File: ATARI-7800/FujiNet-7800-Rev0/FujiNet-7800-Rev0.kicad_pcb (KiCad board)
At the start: 6 copper layers, 72.4 x 115 mm, 135 parts, among them J1 Atari7800_Cart_Edge_32, J2 DBG UART, J3 microSD, J4 USB-C, Q1 2N7002, Q2 AO3401A, SW1 RESET, SW2 BOOTSEL, SW3 S3_RST, SW4 S3_BOOT, U1 RP2354B, U10 AP63203WU, U11 AP2112K-3.3, U2 74HCT14, U3 74HCT00, U4 74HCT20, U5 74HCT20, U6 AS6C4008-55TIN, U7 ESP32-S3-WROOM-1-N16R8, U8 CP2102N-A02-GQFN28, U9 UMH3N, Y1 12MHz

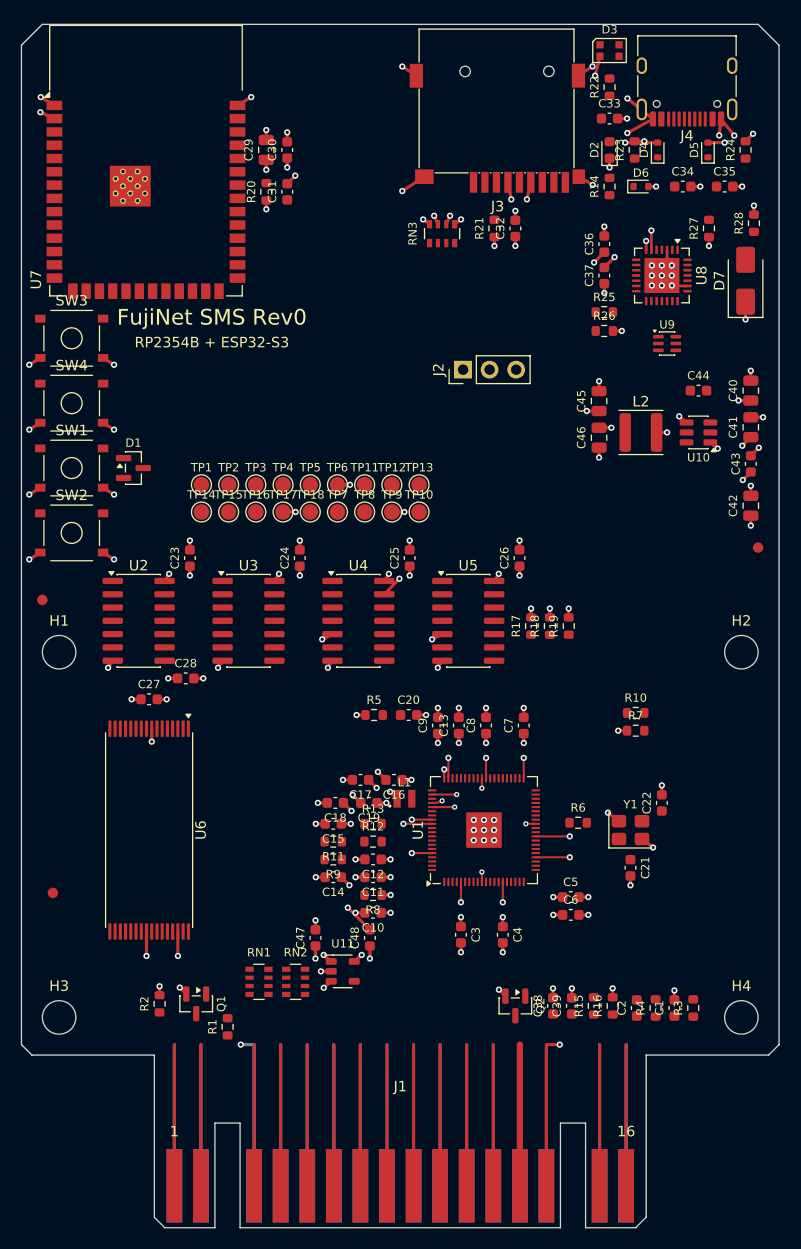
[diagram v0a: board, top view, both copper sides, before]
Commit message: ATARI-7800 Rev0: route the board, JLCPCB + PCBWay packages, layout review
- Routed 6-layer board: 117 nets; DRC 0/0/0 at every severity with schematic
  parity; check_vias clean. The D0-D7 100R packs now face the RP (rotation
  180, RN1 at x 85.5): with them the other way round, every route left
  RP_D5 open. route_board.sh defaults to the settings that routed it
  (12 Freerouting passes, hybrid strategy).
- Fab packages from one gerber set: exports/jlcpcb (BOM, CPL with measured
  rotations) and exports/pcbway (MPN BOM, centroid, assembly drawing).
- tools/audit/check_gerbers.py checks the fab zips against edge_geom.py:
  slots, both finger faces, mask windows, nothing in the tab. It runs in
  build_all.sh and run_pcb_audit.sh.
- Design review Part 2: routing, the variant runs, and the triage of every
  layout finding. README rewritten for the board, ordering and bring-up.
- R_HALT 10k on the board (sync_pcb_sheets now syncs value, MPN, LCSC and
  description). The audio level resistor is no longer marked provisional.
- Fixes:
  - check_vias tests round pads as circles;
  - gen_sch writes the right top-level sheet (it was the NES template's);
  - the silkscreen title read "FujiNet SMS Rev0";
  - the TS-1187A buttons get a 3D model (the TL3342's) in the library too;
  - PCBWay BOM lines describe the part, not one instance's function;
  - the unused placement variant B is dropped; the tab depth moves into
    edge_geom.

Co-Authored-By: Claude Opus 5.5 <noreply@anthropic.com>
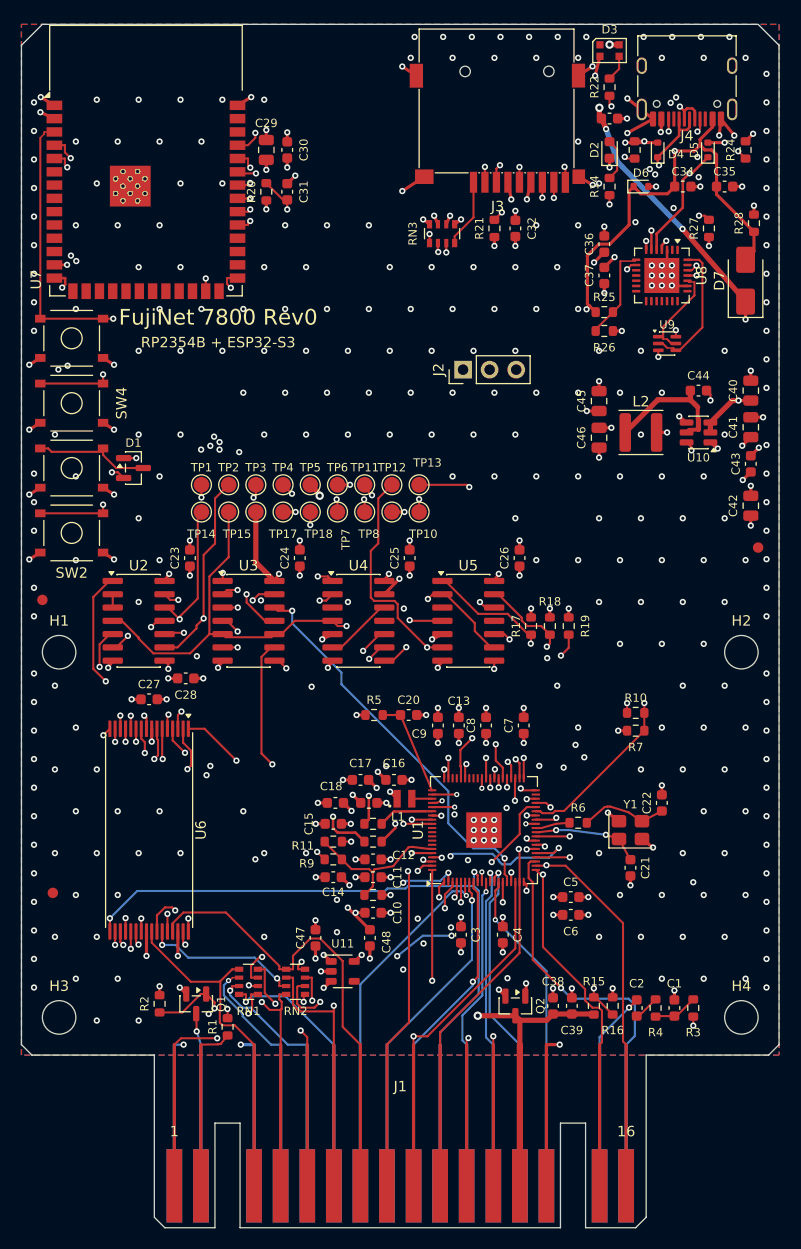
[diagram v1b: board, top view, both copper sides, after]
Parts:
- R1: value 1k -> 10k
- moved RN1 1.00 mm to (85.5, 126.5), turned to 180 degrees
- turned RN2 to 180 degrees
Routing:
- net /PHI2: track 10.2 -> 130.8 mm, vias 0 -> 4
- net /RW: track 10.2 -> 129.7 mm, vias 0 -> 7
- net VBUS: track 0.00 -> 114.3 mm, vias 0 -> 4
- net /S3_EN: track 0.00 -> 109.5 mm, vias 0 -> 4
- net /A12: track 10.2 -> 111.9 mm, vias 0 -> 4
- net /HALT_RP: track 0.00 -> 95.9 mm, vias 0 -> 3
- net /RUN_CTL: track 0.00 -> 93.3 mm, vias 0 -> 2
- net /A15: track 10.2 -> 101.5 mm, vias 0 -> 3
- net /A13: track 10.2 -> 99.9 mm, vias 0 -> 2
- net /glue/VSENSE: track 0.00 -> 85.8 mm, vias 0 -> 3
- net /BOOTSEL_CTL: track 0.00 -> 82.4 mm, vias 0 -> 3
- net /edge/EAUDIO: track 10.2 -> 90.9 mm, vias 0 -> 2
- net /rp2354b/RUN: track 0.00 -> 79.6 mm, vias 0 -> 3
- net /A11: track 10.2 -> 87.0 mm, vias 0 -> 3
- net /USB_DP: track 0.00 -> 76.5 mm, vias 0 -> 5
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- added copper zone on B.Cu, net GND
- added copper zone on F.Cu, net GND
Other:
- board text added: "FujiNet 7800 Rev0"
- board text removed: "FujiNet SMS Rev0"

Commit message: 7800 Rev0: fix the microSD / USB-C alignment (J4 to the board edge, 3D models)
The same defect as NES Rev0: every cart copies the same HRO USB-C and SOFNG
TF-015 footprints and set_models.py rows.

- J4's shell face sat 1.35 mm inside the top edge, where a plug's overmold
  meets the PCB before the plug mates. HRO's recommended layout puts the
  edge at footprint y +3.19 (face 0.46 mm past it): J4 moves (127.4, 40)
  -> (127.4, 38.2). tools/usbc_to_edge.py does it without a re-route: the
  D- tie and its via move with J4 (the via's In3.Cu segment stretches),
  eight 1.8 mm F.Cu stubs join the new pad centres to the old ones, and
  four GND stitching vias under the new pads / slots go. Front silk past
  the edge dropped; a Dwgs.User line marks HRO's edge.
- J4's 3D model: offset (0, -1.045, 0), not (0, +1.42, 0) (KiCad applies
  it after the rotation; the LCSC origin is the front shield legs).
- J3's 3D model: offset (-0.9, -5.5, 0), not (0, 0, 0) (the LCSC origin
  is the card centre on the peg line). J3's copper and position unchanged.

KiCad DRC at every severity with schematic parity on the saved fills:
0 / 0 / 0. check_vias, check_plane_shorts (both zips) and check_gerbers
clean. Drill changes: J4's slots and pegs, the removed vias, the moved
D- via; the CPLs change J4's Y only. placement.py, set_models.py and both
library footprints carry the fix for a LAYOUT=1 rebuild.

Co-Authored-By: Claude Opus 5.5 <noreply@anthropic.com>
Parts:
- moved J4 1.80 mm to (127.4, 38.2)
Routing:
- net GND: track 138.0 -> 141.6 mm, vias 362 -> 358
- net VBUS: track 114.3 -> 117.9 mm
- net /usb-uart/UBRG_DP: track 15.8 -> 19.4 mm
- net /usb-uart/CC2: track 9.61 -> 11.4 mm
- net /usb-uart/CC1: track 11.7 -> 13.5 mm
- net /usb-uart/UBRG_DM: track 21.1 -> 22.7 mm
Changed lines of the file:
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@@
 	(footprint "FujiNet-7800:USB_C_Receptacle_HRO_TYPE-C-31-M-12"
 		(layer "F.Cu")
-		(at 127.4 40 180)
-		(descr "USB Type-C receptacle for USB 2.0 and PD, http://www.krhro.com/uploads/soft/180320/1-1P320120243.pdf")
+		(at 127.4 38.2 180)
+		(descr "USB Type-C receptacle for USB 2.0 and PD, http://www.krhro.com/uploads/soft/180320/1-1P320120243.pdf; PCB edge at y 3.19 (HRO recommended layout: 5.79 mm in front of the pegs), the shell face overhangs it by 0.46 mm")
 		(tags "usb usb-c 2.0 pd")
 		(property "Reference" "J4"
@@
 		(duplicate_pad_numbers_are_jumpers no)
 		(fp_line
-			(start 4.7 2)
-			(end 4.7 3.9)
-			(stroke
-				(width 0.12)
-				(type solid)
-			)
-			(layer "F.SilkS")
-		)
-		(fp_line
 			(start 4.7 -1.9)
 			(end 4.7 0.1)
@@
 		)
 		(fp_line
-			(start -4.7 3.9)
-			(end 4.7 3.9)
-			(stroke
-				(width 0.12)
-				(type solid)
-			)
-			(layer "F.SilkS")
-		)
-		(fp_line
-			(start -4.7 2)
-			(end -4.7 3.9)
+			(start -4.7 -1.9)
+			(end -4.7 0.1)
 			(stroke
 				(width 0.12)
@@
 		)
 		(fp_line
-			(start -4.7 -1.9)
-			(end -4.7 0.1)
+			(start -5.32 3.19)
+			(end 5.32 3.19)
 			(stroke
-				(width 0.12)
-				(type solid)
+				(width 0.1)
+				(type dash)
 			)
-			(layer "F.SilkS")
+			(layer "Dwgs.User")
 		)
 		(fp_line
@@
 		(model "${KIPRJMOD}/3d/USB-C_HRO_TYPE-C-31-M-12.step"
 			(offset
-				(xyz 0 1.42 0)
+				(xyz 0 -1.045 0)
 			)
 			(scale
@@
 		(model "${KIPRJMOD}/3d/TF-015.step"
 			(offset
-				(xyz 0 0 0)
+				(xyz -0.9 -5.5 0)
 			)
 			(scale
@@
 	)
 	(segment
+		(start 124.15 42.245)
+		(end 124.15 44.045)
+		(width 0.3)
+		(layer "F.Cu")
+		(net "GND")
+	)
+	(segment
 		(start 98.625 107.2)
 		(end 97.857 106.432)
@@
 	)
 	(segment
+		(start 130.65 42.245)
+		(end 130.65 44.045)
+		(width 0.3)
+		(layer "F.Cu")
+		(net "GND")
+	)
+	(segment
 		(start 120.9 111.15)
 		(end 119.844 110.334)
@@
 	)
 	(via
-		(at 125.84 42.5)
-		(size 0.6)
-		(drill 0.3)
-		(layers "F.Cu" "B.Cu")
-		(locked yes)
-		(net "GND")
-	)
-	(via
 		(at 133 86.2)
 		(size 0.6)
@@
 	)
 	(via
-		(at 126.36 41.98)
-		(size 0.6)
-		(drill 0.3)
-		(layers "F.Cu" "B.Cu")
-		(locked yes)
-		(net "GND")
-	)
-	(via
 		(at 101.37 36.2)
 		(size 0.6)
@@
 	)
 	(via
-		(at 123.26 36.2)
-		(size 0.6)
-		(drill 0.3)
-		(layers "F.Cu" "B.Cu")
-		(locked yes)
-		(net "GND")
-	)
-	(via
 		(at 77 54.2)
 		(size 0.6)
@@
 	)
 	(via
-		(at 131.46 36.2)
-		(size 0.6)
-		(drill 0.3)
-		(layers "F.Cu" "B.Cu")
-		(locked yes)
-		(net "GND")
-	)
-	(via
 		(at 105 70.2)
 		(size 0.6)
@@
 	)
 	(segment
+		(start 124.95 42.245)
+		(end 124.95 44.045)
+		(width 0.3)
+		(layer "F.Cu")
+		(net "VBUS")
+	)
+	(segment
 		(start 122.9895 51.1895)
 		(end 125.5355 51.1895)
@@
 	)
 	(segment
+		(start 129.85 42.245)
+		(end 129.85 44.045)
+		(width 0.3)
+		(layer "F.Cu")
+		(net "VBUS")
+	)
+	(segment
 		(start 112.0247 127.7878)
 		(end 112.0247 126.6457)
@@
 	)
 	(segment
+		(start 128.65 42.245)
+		(end 128.65 44.045)
+		(width 0.2)
+		(layer "F.Cu")
+		(net "/usb-uart/CC1")
+	)
+	(segment
 		(start 121.6119 47.825)
 		(end 121.4515 47.6646)
@@
 	)
 	(segment
+		(start 126.65 42.245)
+		(end 126.65 44.045)
+		(width 0.25)
+		(layer "F.Cu")
+		(net "/usb-uart/UBRG_DP")
+	)
+	(segment
 		(start 127.65 44.045)
 		(end 127.65 44.8409)
@@
 	)
 	(segment
+		(start 127.65 42.245)
+		(end 127.65 44.045)
+		(width 0.25)
+		(layer "F.Cu")
+		(net "/usb-uart/UBRG_DP")
+	)
+	(segment
 		(start 127.4 45.0909)
 		(end 126.65 45.0909)
@@
 	)
 	(segment
-		(start 127.15 43.29)
-		(end 127.4011 43.0389)
+		(start 127.15 41.49)
+		(end 127.4011 41.2389)
 		(width 0.25)
 		(layer "F.Cu")
@@
 	)
 	(segment
-		(start 126.7196 42.8596)
-		(end 127.15 43.29)
+		(start 126.7196 41.0596)
+		(end 127.15 41.49)
 		(width 0.25)
 		(layer "F.Cu")
@@
 	)
 	(segment
-		(start 127.4011 43.0389)
-		(end 127.9163 43.0389)
+		(start 127.4011 41.2389)
+		(end 127.9163 41.2389)
 		(width 0.25)
 		(layer "F.Cu")
@@
 	)
 	(segment
-		(start 128.15 43.2726)
-		(end 128.15 44.045)
+		(start 128.15 41.4726)
+		(end 128.15 42.245)
 		(width 0.25)
 		(layer "F.Cu")
@@
 	)
 	(segment
-		(start 127.15 44.045)
-		(end 127.15 43.29)
+		(start 127.15 42.245)
+		(end 127.15 41.49)
 		(width 0.25)
 		(layer "F.Cu")
@@
 	)
 	(segment
-		(start 127.9163 43.0389)
-		(end 128.15 43.2726)
+		(start 127.9163 41.2389)
+		(end 128.15 41.4726)
 		(width 0.25)
 		(layer "F.Cu")
@@
 	)
 	(via
-		(at 126.7196 42.8596)
+		(at 126.7196 41.0596)
 		(size 0.6)
 		(drill 0.3)
@@
 	(segment
 		(start 127.6376 43.7776)
-		(end 126.7196 42.8596)
+		(end 126.7196 41.0596)
 		(width 0.25)
 		(layer "In3.Cu")
@@
 	)
 	(segment
+		(start 125.65 42.245)
+		(end 125.65 44.045)
+		(width 0.2)
+		(layer "F.Cu")
+		(net "/usb-uart/CC2")
+	)
+	(segment
